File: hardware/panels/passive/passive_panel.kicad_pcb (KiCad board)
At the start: 2 copper layers, 93 x 93 mm, 82 parts, among them J1 i/O, J2 Conn 1, J3 Conn 2

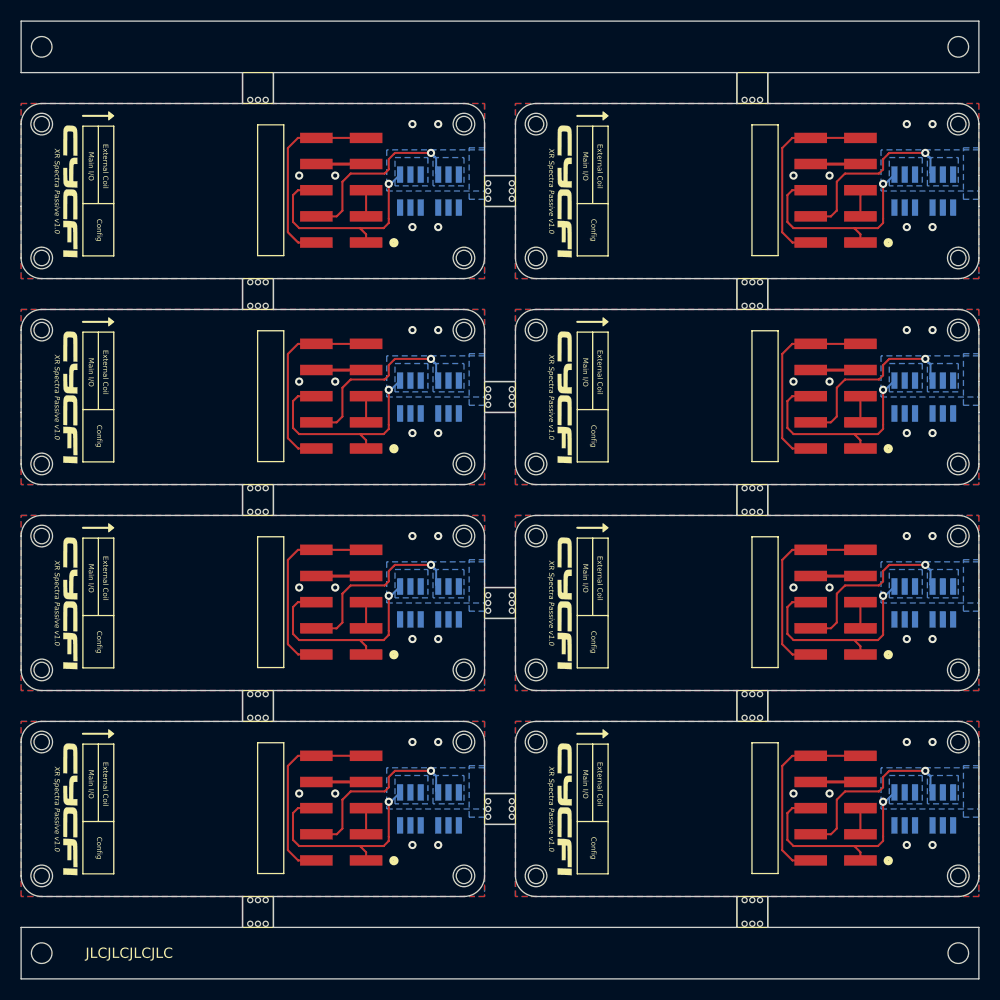
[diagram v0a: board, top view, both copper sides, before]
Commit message: Preamp, Tone Block, Passive, and Bobbin Panel updates
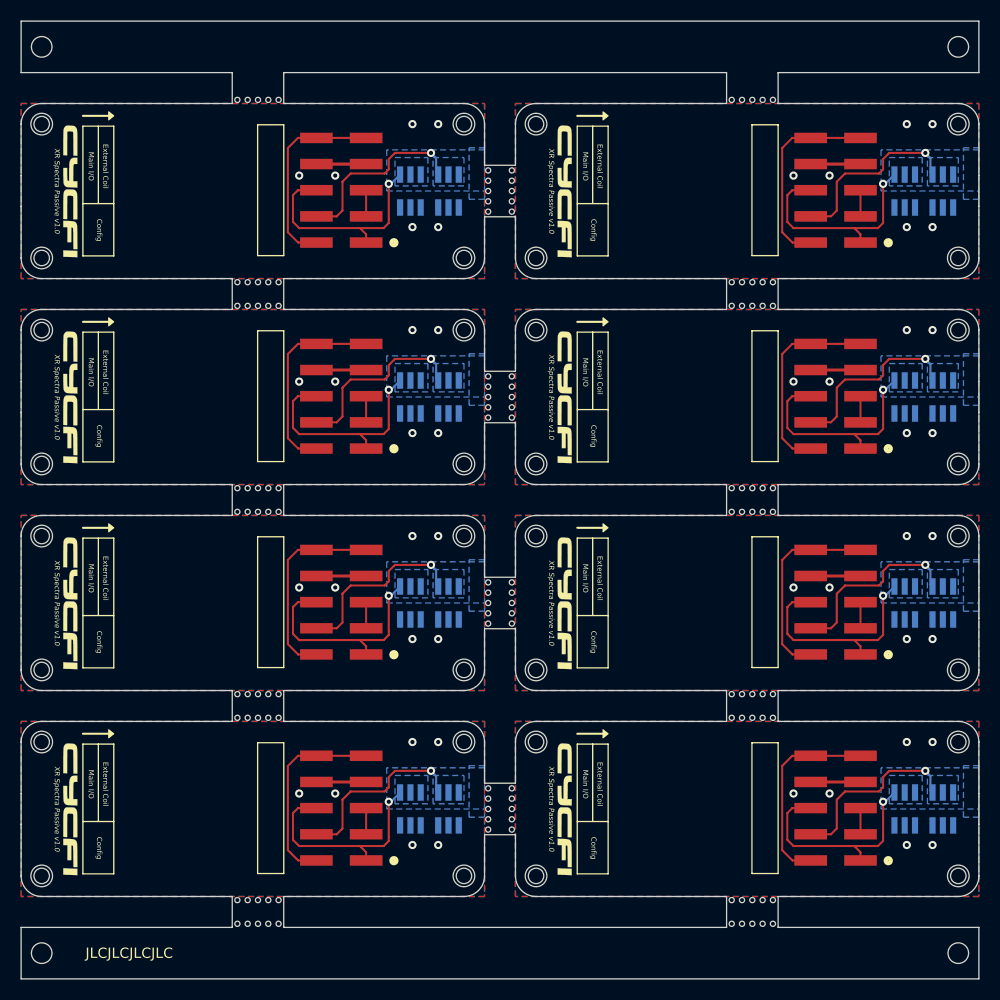
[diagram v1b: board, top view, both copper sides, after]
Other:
- outline, holes or cut-outs redrawn
